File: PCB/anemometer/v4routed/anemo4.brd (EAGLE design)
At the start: 100 x 80 mm, 66 parts, among them IC1 AD8223, IC2 AD8223, IC3 AD8223, IC4 AD8223, IC6 TL072D, J1 RJ12STRAIGHT-I2C, J2 RJ12STRAIGHT-I2C, T1 BC846, T2 BC846, T3 BC846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

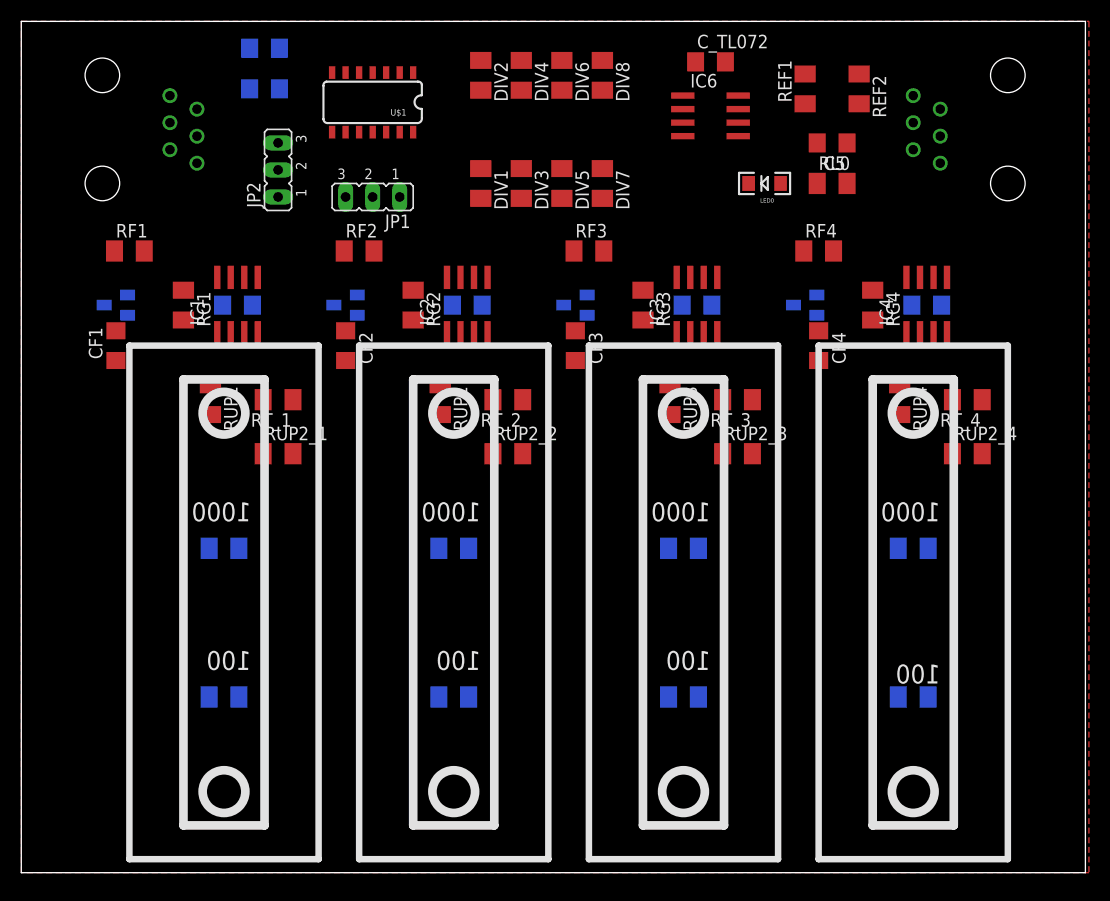
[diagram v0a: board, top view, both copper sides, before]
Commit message: routed anemometer and integrated bertha with ground planes and separate analog and digital ground. ready for fabrication
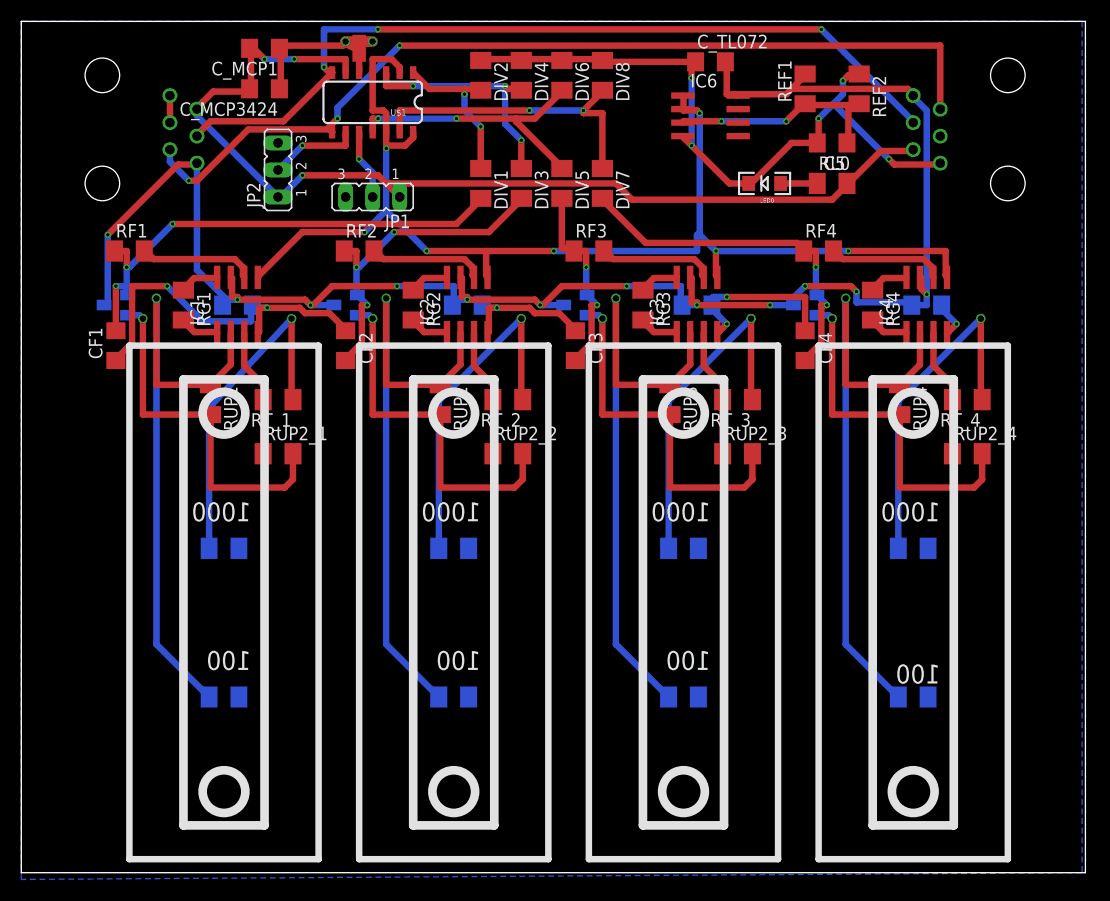
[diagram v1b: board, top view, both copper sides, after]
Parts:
- added U$2: STARGND, lpatiny:STAR
- DIV1, DIV3, DIV5, DIV7: value 20k -> 10k
- REF1: value 100k -> 200k
- RG1, RG2, RG3, RG4: value 500 -> 91
- T1, T2, T3, T4: value BC846 -> (none); device transistor:SOT23 -> transistor:SOT23-BEC
- moved CF4 1.27 mm to (73.7, 49.5)
- flipped C_MCP1 to the top
- flipped C_MCP3424 to the top
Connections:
- new net DGND: U$1.5, U$2.DGND
- net GND: now also U$2.AGND, U$2.GND; no longer U$1.12, U$1.14, U$1.2, U$1.4, U$1.5
- net N$11: now also T2.E; no longer T2.2
- net N$12: now also T3.E; no longer T3.2
- net N$13: now also T4.E; no longer T4.2
- net N$9: now also T1.E; no longer T1.2
- net OUT1: now also T1.B; no longer T1.1
- net OUT2: now also T2.B; no longer T2.1
- net OUT3: now also T3.B; no longer T3.1
- net OUT4: now also T4.B; no longer T4.1
- net REF: now also U$1.12, U$1.14, U$1.2, U$1.4
- net VCC: now also T1.C, T2.C, T3.C, T4.C; no longer T1.3, T2.3, T3.3, T4.3
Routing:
- net VCC: track 0.00 -> 165.9 mm, vias 0 -> 12
- net GND: track 0.00 -> 151.8 mm, vias 0 -> 13
- net REF: track 0.00 -> 115.1 mm, vias 0 -> 7
- net 5V: track 0.00 -> 97.2 mm, vias 0 -> 3
- net SCL: track 0.00 -> 86.9 mm, vias 0 -> 3
- net SDA: track 0.00 -> 78.9 mm, vias 0 -> 3
- net IN-4: track 0.00 -> 58.4 mm, vias 0 -> 1
- net IN-2: track 0.00 -> 58.4 mm, vias 0 -> 1
- net IN-3: track 0.00 -> 58.4 mm, vias 0 -> 1
- net IN-1: track 0.00 -> 58.4 mm, vias 0 -> 1
- net OUT1: track 0.00 -> 46.5 mm, vias 0 -> 3
- net N$11: track 0.00 -> 34.3 mm, vias 0 -> 1
- net N$9: track 0.00 -> 34.3 mm, vias 0 -> 1
- net N$13: track 0.00 -> 34.3 mm, vias 0 -> 1
- net N$12: track 0.00 -> 34.3 mm, vias 0 -> 1
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- added copper zone on layer 16, net GND
- removed copper zone on layer 1, net GND

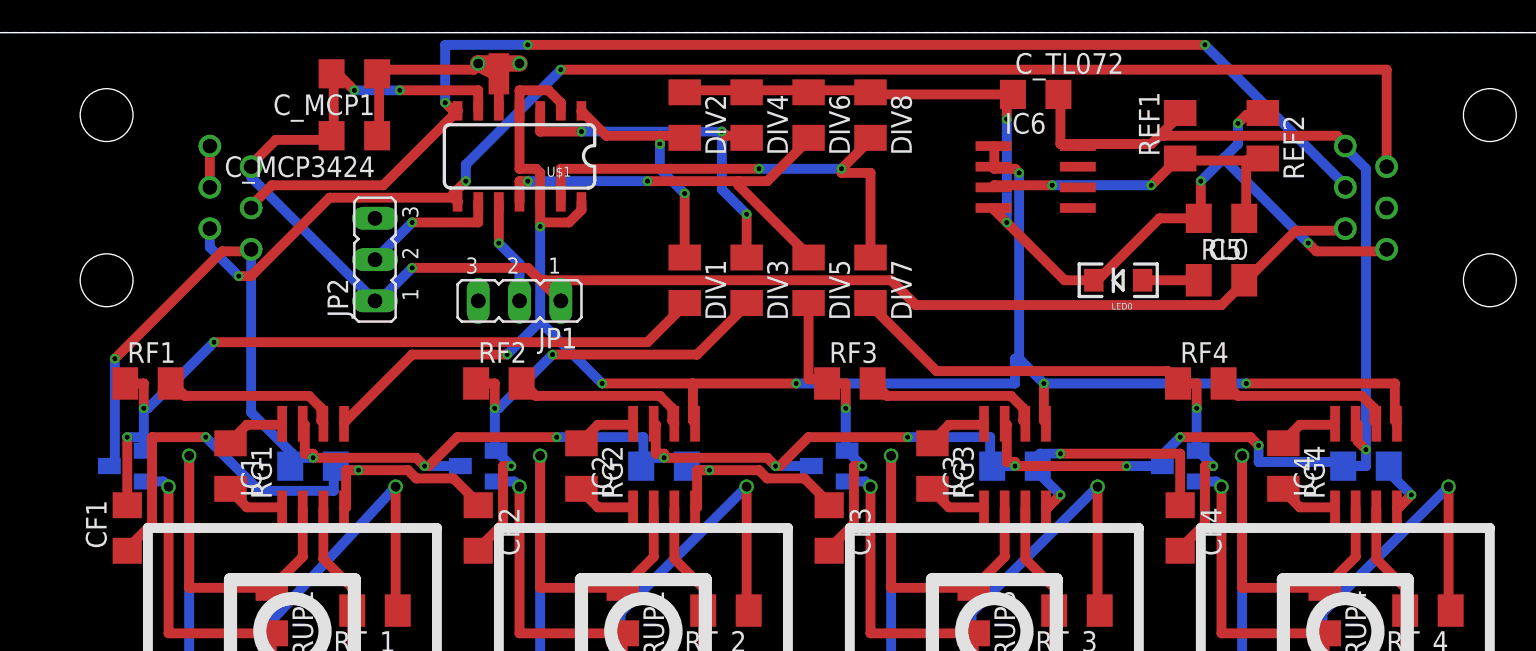
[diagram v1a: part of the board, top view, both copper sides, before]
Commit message: integratedBertha v1.1: adjusted labels to good position. Anemometer: added ferrite bead for vcc decoupling and ground line.
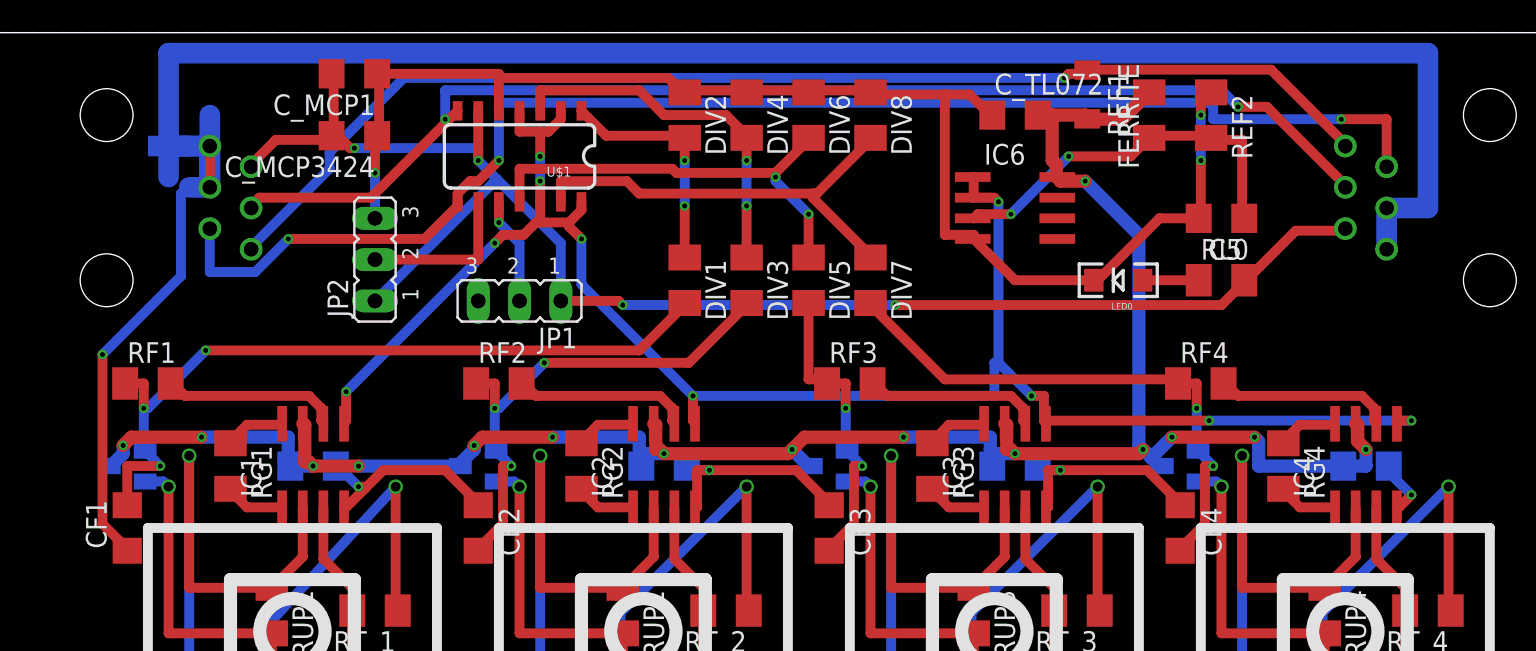
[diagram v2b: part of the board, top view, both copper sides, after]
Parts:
- added FERRITE: 80Ohm, rcl:L3216C
- moved U$2 20.1 mm to (11.4, 73.7), flipped to the bottom, turned to 270 degrees
- moved REF2 3.42 mm to (75.6, 74.9)
- moved REF1 2.29 mm to (71.8, 74.9)
- moved IC6 2.29 mm to (63.5, 69.2)
- moved C_TL072 1.80 mm to (63.5, 74.9)
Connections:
- removed net DGND: U$1.5, U$2.DGND
- new net +12V: FERRITE.1, J1.+12V, J2.+12V
- new net MIXEDGND: J1.GND1, J1.GND2, J2.GND1, J2.GND2, U$2.GND
- net GND: now also U$1.5; no longer J1.GND1, J1.GND2, J2.GND1, J2.GND2, U$2.GND
- net VCC: now also FERRITE.2; no longer J1.+12V, J2.+12V
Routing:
- net MIXEDGND: track 0.00 -> 105.4 mm
- net +12V: track 0.00 -> 74.6 mm, vias 0 -> 1
- net VCC: track 165.9 -> 131.9 mm, vias 12 -> 15
- net GND: track 151.8 -> 164.1 mm, vias 13 -> 8
- net REF: track 115.1 -> 110.2 mm, vias 7 -> 10
- net SDA: track 78.9 -> 75.1 mm, vias 3 -> 2
- net DGND: track 2.92 -> 0.00 mm
- net N$10: track 21.2 -> 23.7 mm
- net 5V: track 97.2 -> 94.9 mm, vias 3 -> 4
- net SIG4: track 29.2 -> 27.5 mm, vias 2 -> 0
- net ADR0: track 8.56 -> 9.90 mm, vias 1 -> 0
- net SCL: track 86.9 -> 85.7 mm
- net SIG1: track 15.2 -> 14.5 mm
- net OUT1: track 46.5 -> 47.1 mm
- net SIG2: vias 3 -> 2

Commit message: added relay card with jumpers. adjusted labels in anemometer
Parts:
- FERRITE: value 80Ohm -> 80R Ferrite
- PT1K_1, PT1K_2, PT1K_3, PT1K_4: value 90.9 -> 909
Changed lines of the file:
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@@
 <grid distance="0.025" unitdist="inch" unit="inch" style="lines" multiple="1" display="yes" altdistance="0.025" altunitdist="inch" altunit="inch"/>
 <layers>
-<layer number="1" name="Top" color="4" fill="1" visible="yes" active="yes"/>
+<layer number="1" name="Top" color="4" fill="1" visible="no" active="yes"/>
 <layer number="16" name="Bottom" color="1" fill="1" visible="yes" active="yes"/>
 <layer number="17" name="Pads" color="2" fill="1" visible="yes" active="yes"/>
@@
 <layer number="19" name="Unrouted" color="6" fill="1" visible="yes" active="yes"/>
 <layer number="20" name="Dimension" color="15" fill="1" visible="yes" active="yes"/>
-<layer number="21" name="tPlace" color="7" fill="1" visible="yes" active="yes"/>
+<layer number="21" name="tPlace" color="7" fill="1" visible="no" active="yes"/>
 <layer number="22" name="bPlace" color="7" fill="1" visible="yes" active="yes"/>
-<layer number="23" name="tOrigins" color="15" fill="1" visible="yes" active="yes"/>
-<layer number="24" name="bOrigins" color="15" fill="1" visible="no" active="yes"/>
+<layer number="23" name="tOrigins" color="15" fill="1" visible="no" active="yes"/>
+<layer number="24" name="bOrigins" color="15" fill="1" visible="yes" active="yes"/>
 <layer number="25" name="tNames" color="7" fill="1" visible="no" active="yes"/>
 <layer number="26" name="bNames" color="7" fill="1" visible="no" active="yes"/>
 <layer number="27" name="tValues" color="7" fill="1" visible="no" active="yes"/>
-<layer number="28" name="bValues" color="7" fill="1" visible="no" active="yes"/>
+<layer number="28" name="bValues" color="7" fill="1" visible="yes" active="yes"/>
 <layer number="29" name="tStop" color="7" fill="3" visible="no" active="yes"/>
 <layer number="30" name="bStop" color="7" fill="6" visible="no" active="yes"/>
@@
 <element name="RUP2_4" library="resistor" package="M1206" value="100" x="88.9" y="39.37"/>
 <element name="REF1" library="resistor" package="M1206" value="200k" x="71.755" y="74.93" rot="R90"/>
-<element name="REF2" library="resistor" package="M1206" value="100k" x="75.565" y="74.93" rot="R270"/>
+<element name="REF2" library="resistor" package="M1206" value="100k" x="75.565" y="74.93" smashed="yes" rot="R270">
+<attribute name="NAME" x="76.835" y="76.2" size="1.27" layer="25" rot="R270"/>
+<attribute name="VALUE" x="76.835" y="76.835" size="1.27" layer="27" rot="R270"/>
+</element>
 <element name="RT_1" library="resistor" package="M1206" value="90.9" x="24.13" y="44.45" rot="R180"/>
 <element name="RT_2" library="resistor" package="M1206" value="90.9" x="45.72" y="44.45" rot="R180"/>
@@
 <element name="C_MCP1" library="rcl" package="C1206" value="10µ" x="22.86" y="77.47" rot="R180"/>
 <element name="U$1" library="mcp3424" package="14LDSOIC" value="MCP3424(SO14)" x="33.02" y="72.39" rot="R270"/>
-<element name="PT1K_1" library="resistor" package="M1206" value="90.9" x="19.05" y="30.48" rot="MR0"/>
+<element name="PT1K_1" library="resistor" package="M1206" value="909" x="19.05" y="30.48" rot="MR0"/>
 <element name="PT100_1" library="resistor" package="M1206" value="90.9" x="19.05" y="16.51" rot="MR0"/>
 <element name="PT100_2" library="resistor" package="M1206" value="90.9" x="40.64" y="16.51" rot="MR0"/>
 <element name="PT100_3" library="resistor" package="M1206" value="90.9" x="62.23" y="16.51" rot="MR0"/>
 <element name="PT100_4" library="resistor" package="M1206" value="90.9" x="83.82" y="16.51" rot="MR0"/>
-<element name="PT1K_2" library="resistor" package="M1206" value="90.9" x="40.64" y="30.48" rot="MR0"/>
-<element name="PT1K_3" library="resistor" package="M1206" value="90.9" x="62.23" y="30.48" rot="MR0"/>
-<element name="PT1K_4" library="resistor" package="M1206" value="90.9" x="83.82" y="30.48" rot="MR0"/>
+<element name="PT1K_2" library="resistor" package="M1206" value="909" x="40.64" y="30.48" rot="MR0"/>
+<element name="PT1K_3" library="resistor" package="M1206" value="909" x="62.23" y="30.48" rot="MR0"/>
+<element name="PT1K_4" library="resistor" package="M1206" value="909" x="83.82" y="30.48" rot="MR0"/>
 <element name="IC1" library="analog-devices" package="SO8" value="AD8223" x="20.32" y="53.34">
 <attribute name="OC_NEWARK" value="05F7109" x="20.32" y="53.34" size="1.778" layer="27" display="off"/>
@@
 <element name="RL0" library="resistor" package="M1206" value="1K" x="76.2" y="64.77"/>
 <element name="LED0" library="SparkFun" package="LED-1206" value="" x="69.85" y="64.77" rot="R180"/>
-<element name="FERRITE" library="rcl" package="L3216C" value="80Ohm" x="67.945" y="76.2" rot="R270"/>
+<element name="FERRITE" library="rcl" package="L3216C" value="80R Ferrite" x="67.945" y="76.2" smashed="yes" rot="R270">
+<attribute name="NAME" x="69.85" y="78.105" size="1.27" layer="25" rot="R270"/>
+<attribute name="VALUE" x="69.85" y="70.485" size="1.27" layer="27" rot="R90"/>
+</element>
 <element name="U$2" library="lpatiny" package="STAR" value="STARGND" x="11.43" y="73.66" rot="MR270"/>
 </elements>

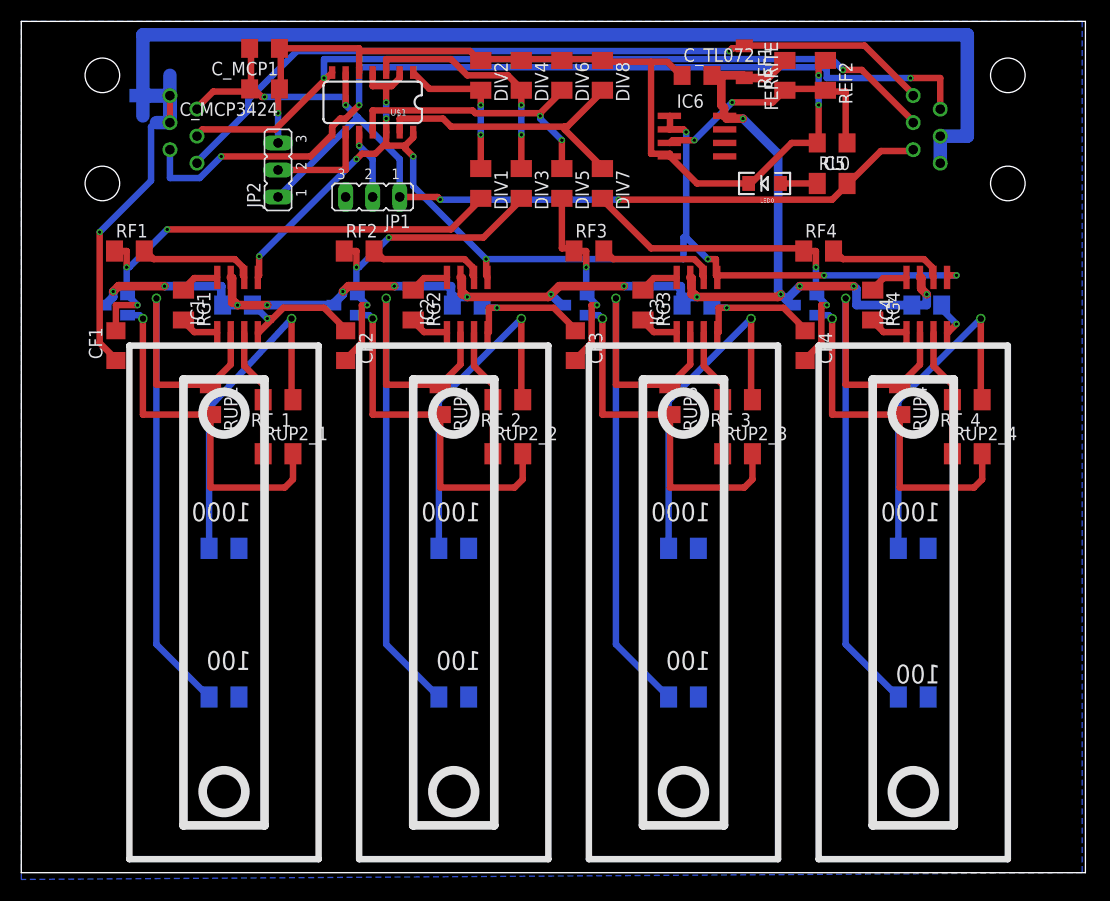
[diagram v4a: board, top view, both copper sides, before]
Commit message: corrected silk layer in anemometer
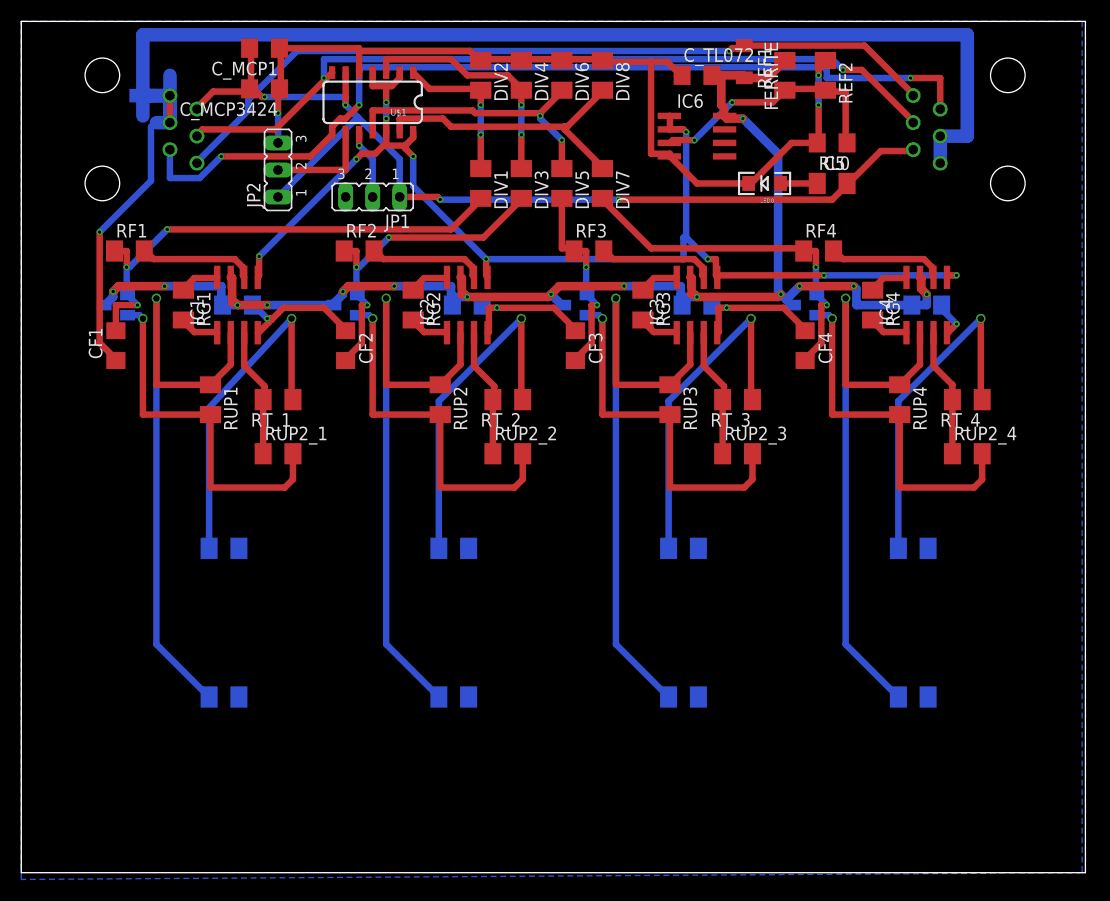
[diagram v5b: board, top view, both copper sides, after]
